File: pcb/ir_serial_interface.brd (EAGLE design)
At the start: 41.6 x 43.2 mm, 22 parts, among them IC1 PIC18F2550_28W, T1 SFH303

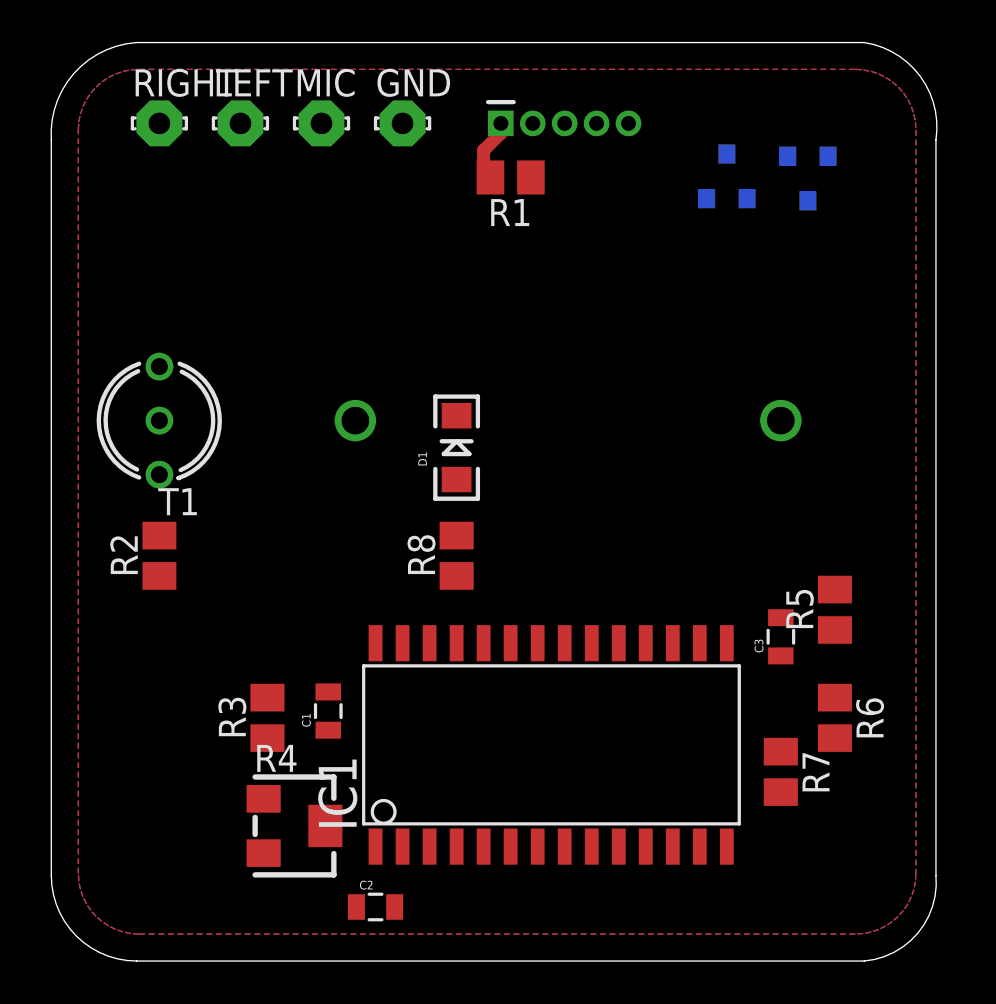
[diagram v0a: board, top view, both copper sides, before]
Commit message: RS232_TX working
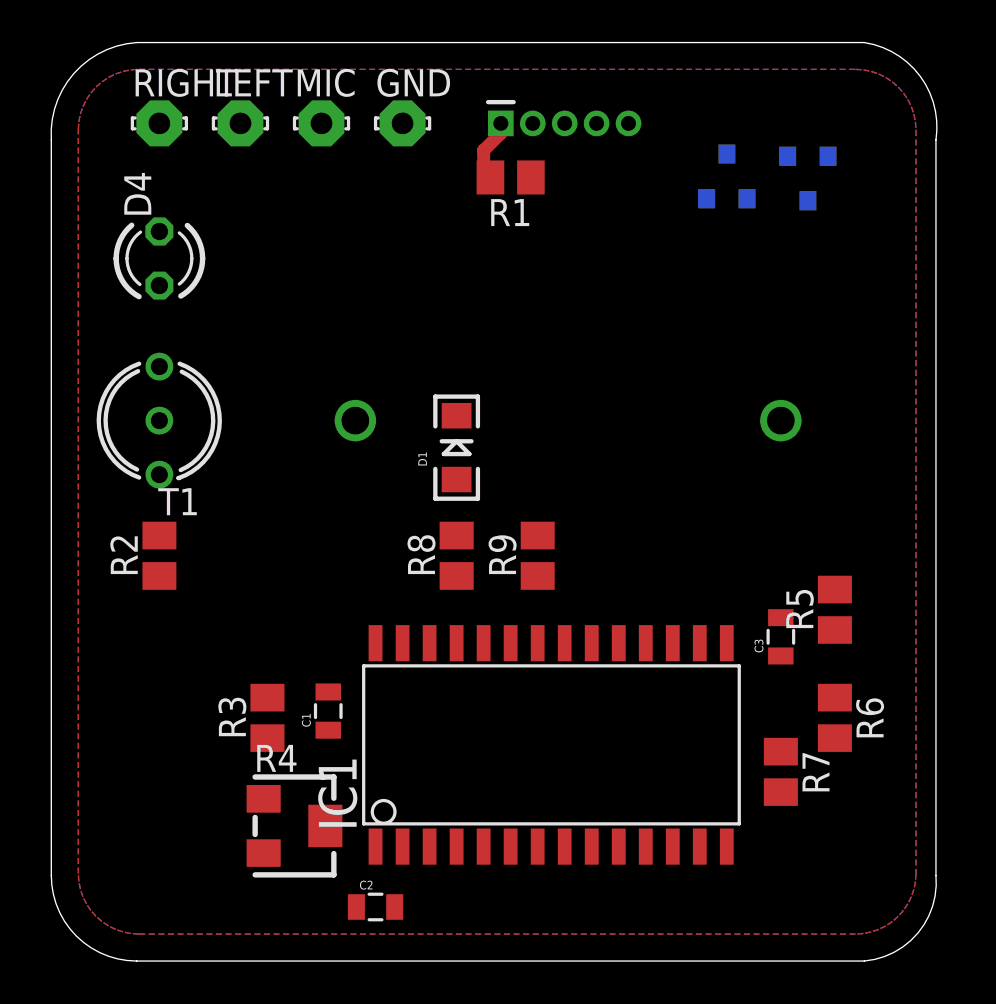
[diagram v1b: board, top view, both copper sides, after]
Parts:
- added D4: IR, led:LED3MM
- added R9: 190, resistor:M0805
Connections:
- new net N$14: D4.A, R9.2
- new net N$15: IC1.22, R9.1
- net GND: now also D4.K
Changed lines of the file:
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@@
 <?xml version="1.0" encoding="utf-8"?>
 <!DOCTYPE eagle SYSTEM "eagle.dtd">
-<eagle version="6.5.0">
+<eagle version="6.6.0">
 <drawing>
 <settings>
@@
 <element name="D3" library="SparkFun-DiscreteSemi" package="SOT23-3" value="" x="53.34" y="62.23" rot="MR0"/>
 <element name="R4" library="resistor" package="RTRIM3214W" value="200k" x="33.02" y="31.75" rot="R270"/>
+<element name="R9" library="resistor" package="M0805" value="190" x="44.45" y="44.45" rot="R90"/>
+<element name="D4" library="led" package="LED3MM" value="IR" x="26.67" y="58.42" rot="R90"/>
 </elements>
 <signals>
@@
 <contactref element="D3" pad="1"/>
 <contactref element="R4" pad="1"/>
+<contactref element="D4" pad="K"/>
+<wire x1="45.72" y1="64.77" x2="54.29" y2="61.23" width="0" layer="19" extent="16-16"/>
+<wire x1="38.1" y1="64.77" x2="45.72" y2="64.77" width="0" layer="19" extent="1-1"/>
+<wire x1="40.64" y1="51.03" x2="38.1" y2="64.77" width="0" layer="19" extent="1-1"/>
+<wire x1="48.26" y1="40.34" x2="40.64" y2="51.03" width="0" layer="19" extent="1-1"/>
+<wire x1="58.42" y1="40.96" x2="48.26" y2="40.34" width="0" layer="19" extent="1-1"/>
 <wire x1="58.42" y1="37.78" x2="58.42" y2="40.96" width="0" layer="19" extent="1-1"/>
-<wire x1="48.26" y1="40.34" x2="58.42" y2="40.96" width="0" layer="19" extent="1-1"/>
-<wire x1="40.64" y1="51.03" x2="48.26" y2="40.34" width="0" layer="19" extent="1-1"/>
-<wire x1="38.1" y1="64.77" x2="40.64" y2="51.03" width="0" layer="19" extent="1-1"/>
 <wire x1="26.67" y1="43.5" x2="40.64" y2="51.03" width="0" layer="19" extent="1-1"/>
 <wire x1="31.57" y1="33.025" x2="26.67" y2="43.5" width="0" layer="19" extent="1-1"/>
 <wire x1="35.93" y1="27.94" x2="31.57" y2="33.025" width="0" layer="19" extent="1-1"/>
+<wire x1="26.67" y1="59.69" x2="35.93" y2="27.94" width="0" layer="19" extent="1-1"/>
 </signal>
 <signal name="N$1">
@@
 <wire x1="53.34" y1="63.33" x2="56.2" y2="63.23" width="0" layer="19" extent="16-16"/>
 </signal>
+<signal name="N$14">
+<contactref element="D4" pad="A"/>
+<contactref element="R9" pad="2"/>
+<wire x1="26.67" y1="57.15" x2="44.45" y2="45.4" width="0" layer="19" extent="1-1"/>
+</signal>
+<signal name="N$15">
+<contactref element="R9" pad="1"/>
+<contactref element="IC1" pad="22"/>
+<wire x1="44.45" y1="43.5" x2="44.45" y2="40.34" width="0" layer="19" extent="1-1"/>
+</signal>
 </signals>

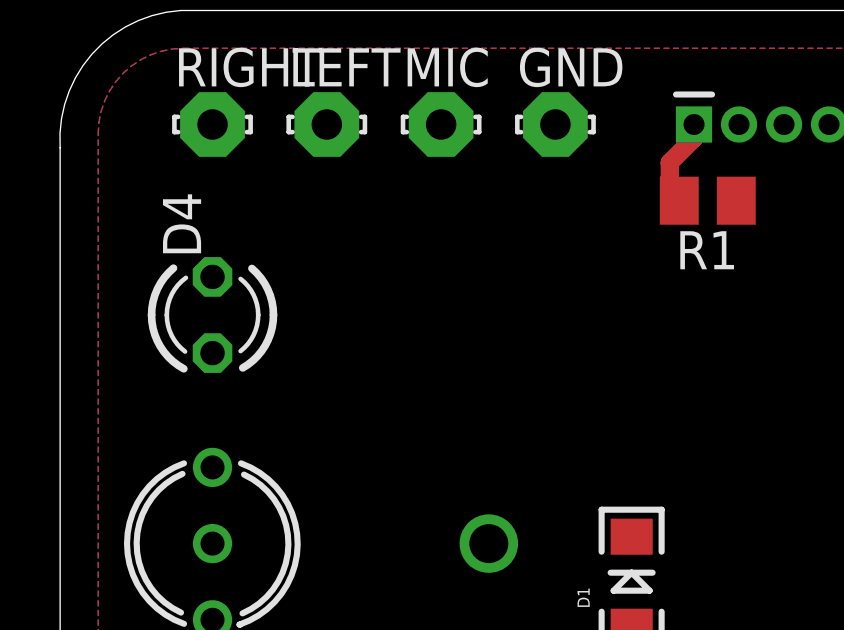
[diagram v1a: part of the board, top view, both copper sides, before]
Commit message: PCB: R channel enables MeterLogger
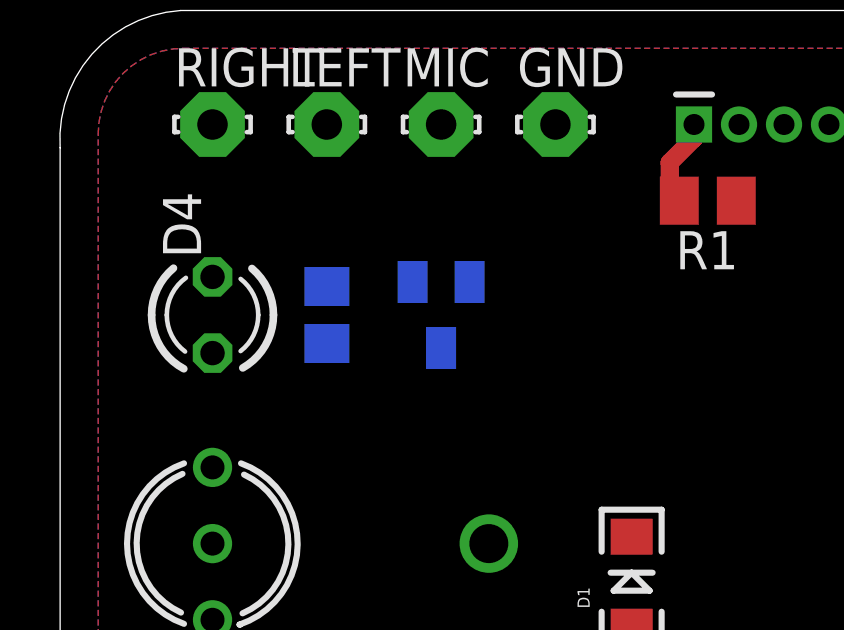
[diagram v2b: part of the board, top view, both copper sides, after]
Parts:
- added C4: (no value), rcl:C0805
- added Q1: BSS123, transistor-small-signal:SOT23
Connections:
- new net N$16: BAT1.1, Q1.3
- new net N$17: C4.1, Q1.1, RIGHT.MP
- net +5V: now also Q1.2; no longer BAT1.1
- net GND: now also C4.2
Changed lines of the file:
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@@
 <grid distance="0.05" unitdist="inch" unit="inch" style="dots" multiple="1" display="no" altdistance="0.025" altunitdist="inch" altunit="inch"/>
 <layers>
-<layer number="1" name="Top" color="4" fill="1" visible="yes" active="yes"/>
-<layer number="16" name="Bottom" color="1" fill="1" visible="no" active="yes"/>
+<layer number="1" name="Top" color="4" fill="1" visible="no" active="yes"/>
+<layer number="16" name="Bottom" color="1" fill="1" visible="yes" active="yes"/>
 <layer number="17" name="Pads" color="2" fill="1" visible="yes" active="yes"/>
 <layer number="18" name="Vias" color="2" fill="1" visible="yes" active="yes"/>
 <layer number="19" name="Unrouted" color="6" fill="1" visible="yes" active="yes"/>
 <layer number="20" name="Dimension" color="15" fill="1" visible="yes" active="yes"/>
-<layer number="21" name="tPlace" color="7" fill="1" visible="yes" active="yes"/>
-<layer number="22" name="bPlace" color="7" fill="1" visible="no" active="yes"/>
-<layer number="23" name="tOrigins" color="15" fill="1" visible="yes" active="yes"/>
-<layer number="24" name="bOrigins" color="15" fill="1" visible="no" active="yes"/>
-<layer number="25" name="tNames" color="7" fill="1" visible="yes" active="yes"/>
-<layer number="26" name="bNames" color="7" fill="1" visible="no" active="yes"/>
-<layer number="27" name="tValues" color="7" fill="1" visible="yes" active="yes"/>
-<layer number="28" name="bValues" color="7" fill="1" visible="no" active="yes"/>
-<layer number="29" name="tStop" color="7" fill="3" visible="yes" active="yes"/>
-<layer number="30" name="bStop" color="7" fill="6" visible="no" active="yes"/>
-<layer number="31" name="tCream" color="7" fill="4" visible="yes" active="yes"/>
-<layer number="32" name="bCream" color="7" fill="5" visible="no" active="yes"/>
-<layer number="33" name="tFinish" color="6" fill="3" visible="yes" active="yes"/>
-<layer number="34" name="bFinish" color="6" fill="6" visible="no" active="yes"/>
-<layer number="35" name="tGlue" color="7" fill="4" visible="yes" active="yes"/>
-<layer number="36" name="bGlue" color="7" fill="5" visible="no" active="yes"/>
-<layer number="37" name="tTest" color="7" fill="1" visible="yes" active="yes"/>
-<layer number="38" name="bTest" color="7" fill="1" visible="no" active="yes"/>
-<layer number="39" name="tKeepout" color="4" fill="11" visible="yes" active="yes"/>
-<layer number="40" name="bKeepout" color="1" fill="11" visible="no" active="yes"/>
-<layer number="41" name="tRestrict" color="4" fill="10" visible="yes" active="yes"/>
-<layer number="42" name="bRestrict" color="1" fill="10" visible="no" active="yes"/>
+<layer number="21" name="tPlace" color="7" fill="1" visible="no" active="yes"/>
+<layer number="22" name="bPlace" color="7" fill="1" visible="yes" active="yes"/>
+<layer number="23" name="tOrigins" color="15" fill="1" visible="no" active="yes"/>
+<layer number="24" name="bOrigins" color="15" fill="1" visible="yes" active="yes"/>
+<layer number="25" name="tNames" color="7" fill="1" visible="no" active="yes"/>
+<layer number="26" name="bNames" color="7" fill="1" visible="yes" active="yes"/>
+<layer number="27" name="tValues" color="7" fill="1" visible="no" active="yes"/>
+<layer number="28" name="bValues" color="7" fill="1" visible="yes" active="yes"/>
+<layer number="29" name="tStop" color="7" fill="3" visible="no" active="yes"/>
+<layer number="30" name="bStop" color="7" fill="6" visible="yes" active="yes"/>
+<layer number="31" name="tCream" color="7" fill="4" visible="no" active="yes"/>
+<layer number="32" name="bCream" color="7" fill="5" visible="yes" active="yes"/>
+<layer number="33" name="tFinish" color="6" fill="3" visible="no" active="yes"/>
+<layer number="34" name="bFinish" color="6" fill="6" visible="yes" active="yes"/>
+<layer number="35" name="tGlue" color="7" fill="4" visible="no" active="yes"/>
+<layer number="36" name="bGlue" color="7" fill="5" visible="yes" active="yes"/>
+<layer number="37" name="tTest" color="7" fill="1" visible="no" active="yes"/>
+<layer number="38" name="bTest" color="7" fill="1" visible="yes" active="yes"/>
+<layer number="39" name="tKeepout" color="4" fill="11" visible="no" active="yes"/>
+<layer number="40" name="bKeepout" color="1" fill="11" visible="yes" active="yes"/>
+<layer number="41" name="tRestrict" color="4" fill="10" visible="no" active="yes"/>
+<layer number="42" name="bRestrict" color="1" fill="10" visible="yes" active="yes"/>
 <layer number="43" name="vRestrict" color="2" fill="10" visible="yes" active="yes"/>
 <layer number="44" name="Drills" color="7" fill="1" visible="yes" active="yes"/>
@@
 <layer number="49" name="Reference" color="7" fill="1" visible="yes" active="yes"/>
 <layer number="50" name="dxf" color="7" fill="1" visible="no" active="no"/>
-<layer number="51" name="tDocu" color="7" fill="1" visible="yes" active="yes"/>
-<layer number="52" name="bDocu" color="7" fill="1" visible="no" active="yes"/>
+<layer number="51" name="tDocu" color="7" fill="1" visible="no" active="yes"/>
+<layer number="52" name="bDocu" color="7" fill="1" visible="yes" active="yes"/>
 <layer number="53" name="tGND_GNDA" color="7" fill="9" visible="no" active="no"/>
 <layer number="54" name="bGND_GNDA" color="1" fill="9" visible="no" active="no"/>
@@
 <layer number="103" name="tMap" color="7" fill="1" visible="yes" active="yes"/>
 <layer number="104" name="Name" color="16" fill="1" visible="yes" active="yes"/>
-<layer number="105" name="tPlate" color="7" fill="1" visible="yes" active="yes"/>
-<layer number="106" name="bPlate" color="7" fill="1" visible="no" active="yes"/>
+<layer number="105" name="tPlate" color="7" fill="1" visible="no" active="yes"/>
+<layer number="106" name="bPlate" color="7" fill="1" visible="yes" active="yes"/>
 <layer number="107" name="Crop" color="7" fill="1" visible="yes" active="yes"/>
 <layer number="108" name="tplace-old" color="10" fill="1" visible="no" active="yes"/>
 <layer number="109" name="ref-old" color="11" fill="1" visible="no" active="yes"/>
 <layer number="116" name="Patch_BOT" color="9" fill="4" visible="yes" active="yes"/>
-<layer number="121" name="_tsilk" color="7" fill="1" visible="yes" active="yes"/>
-<layer number="122" name="_bsilk" color="7" fill="1" visible="no" active="yes"/>
+<layer number="121" name="_tsilk" color="7" fill="1" visible="no" active="yes"/>
+<layer number="122" name="_bsilk" color="7" fill="1" visible="yes" active="yes"/>
 <layer number="125" name="_tNames" color="7" fill="1" visible="yes" active="yes"/>
 <layer number="144" name="Drill_legend" color="7" fill="1" visible="yes" active="yes"/>
@@
 <element name="R9" library="resistor" package="M0805" value="190" x="44.45" y="44.45" rot="R90"/>
 <element name="D4" library="led" package="LED3MM" value="IR" x="26.67" y="58.42" rot="R90"/>
+<element name="Q1" library="transistor-small-signal" package="SOT23" value="BSS123" x="34.29" y="58.42" rot="MR180"/>
+<element name="C4" library="rcl" package="C0805" value="" x="30.48" y="58.42" rot="MR270"/>
 </elements>
 <signals>
@@
 <contactref element="R3" pad="2"/>
 <contactref element="IC1" pad="20"/>
-<contactref element="BAT1" pad="1"/>
+<contactref element="Q1" pad="2"/>
+<wire x1="26.67" y1="50.8" x2="35.24" y2="59.52" width="0" layer="19" extent="16-16"/>
 </signal>
 <signal name="GND">
@@
 <contactref element="R4" pad="1"/>
 <contactref element="D4" pad="K"/>
+<contactref element="C4" pad="2"/>
 <wire x1="45.72" y1="64.77" x2="54.29" y2="61.23" width="0" layer="19" extent="16-16"/>
 <wire x1="38.1" y1="64.77" x2="45.72" y2="64.77" width="0" layer="19" extent="1-1"/>
-<wire x1="40.64" y1="51.03" x2="38.1" y2="64.77" width="0" layer="19" extent="1-1"/>
+<wire x1="30.48" y1="57.47" x2="38.1" y2="64.77" width="0" layer="19" extent="16-16"/>
+<wire x1="26.67" y1="59.69" x2="30.48" y2="57.47" width="0" layer="19" extent="16-16"/>
+<wire x1="40.64" y1="51.03" x2="30.48" y2="57.47" width="0" layer="19" extent="1-16"/>
 <wire x1="48.26" y1="40.34" x2="40.64" y2="51.03" width="0" layer="19" extent="1-1"/>
 <wire x1="58.42" y1="40.96" x2="48.26" y2="40.34" width="0" layer="19" extent="1-1"/>
 <wire x1="58.42" y1="37.78" x2="58.42" y2="40.96" width="0" layer="19" extent="1-1"/>
-<wire x1="26.67" y1="43.5" x2="40.64" y2="51.03" width="0" layer="19" extent="1-1"/>
+<wire x1="26.67" y1="43.5" x2="30.48" y2="57.47" width="0" layer="19" extent="1-16"/>
 <wire x1="31.57" y1="33.025" x2="26.67" y2="43.5" width="0" layer="19" extent="1-1"/>
 <wire x1="35.93" y1="27.94" x2="31.57" y2="33.025" width="0" layer="19" extent="1-1"/>
-<wire x1="26.67" y1="59.69" x2="35.93" y2="27.94" width="0" layer="19" extent="1-1"/>
 </signal>
 <signal name="N$1">
@@
 <contactref element="R9" pad="1"/>
 <contactref element="IC1" pad="22"/>
-<wire x1="44.45" y1="43.5" x2="44.45" y2="40.34" width="0" layer="19" extent="1-1"/>
+<wire x1="44.45" y1="40.34" x2="44.45" y2="43.5" width="0" layer="19" extent="1-1"/>
+</signal>
+<signal name="N$16">
+<contactref element="Q1" pad="3"/>
+<contactref element="BAT1" pad="1"/>
+<wire x1="35.88" y1="50.8" x2="34.29" y2="57.32" width="0" layer="19" extent="16-16"/>
+</signal>
+<signal name="N$17">
+<contactref element="RIGHT" pad="MP"/>
+<contactref element="Q1" pad="1"/>
+<contactref element="C4" pad="1"/>
+<wire x1="26.67" y1="64.77" x2="33.34" y2="59.52" width="0" layer="19" extent="16-16"/>
+<wire x1="30.48" y1="59.37" x2="33.34" y2="59.52" width="0" layer="19" extent="1-16"/>
 </signal>
 </signals>

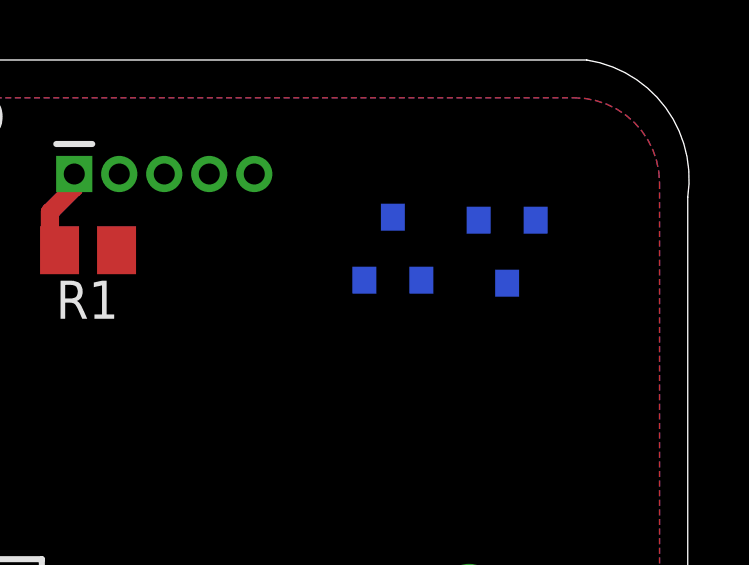
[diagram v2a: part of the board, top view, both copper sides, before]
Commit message: sleep longer after fsk tx
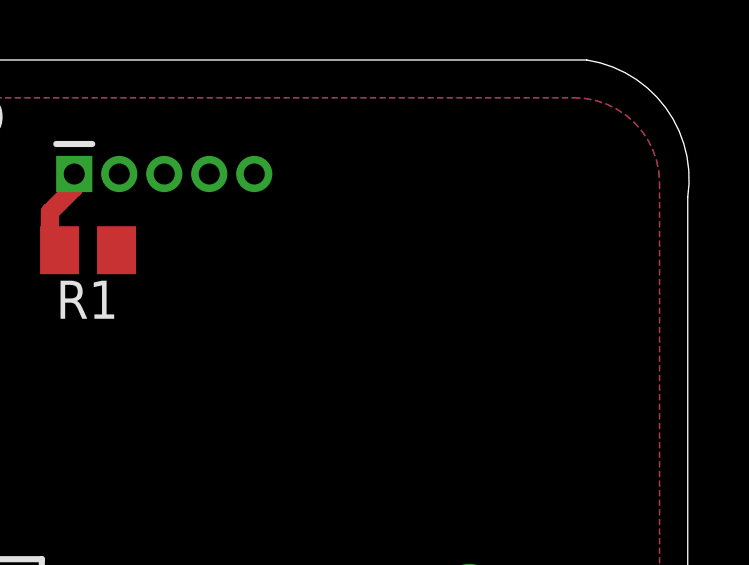
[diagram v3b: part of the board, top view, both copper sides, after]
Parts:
- removed D2, D3: (no value), SparkFun-DiscreteSemi:SOT23-3
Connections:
- removed net N$12: BAT1.2, D2.3
- removed net N$13: D2.1, D3.3
- new net -: BAT1.2
- net GND: no longer D3.1
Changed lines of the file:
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@@
 <element name="R8" library="resistor" package="M0805" value="190" x="40.64" y="44.45" rot="R90"/>
 <element name="BAT1" library="SparkFun-Electromechanical" package="BATTCOM_20MM_PTH" value="20mm coincell" x="55.88" y="50.8" rot="MR0"/>
-<element name="D2" library="SparkFun-DiscreteSemi" package="SOT23-3" value="" x="57.15" y="62.23" rot="MR180"/>
-<element name="D3" library="SparkFun-DiscreteSemi" package="SOT23-3" value="" x="53.34" y="62.23" rot="MR0"/>
 <element name="R4" library="resistor" package="RTRIM3214W" value="200k" x="33.02" y="31.75" rot="R270"/>
 <element name="R9" library="resistor" package="M0805" value="190" x="44.45" y="44.45" rot="R90"/>
@@
 <contactref element="R6" pad="1"/>
 <contactref element="D1" pad="C"/>
-<contactref element="D3" pad="1"/>
 <contactref element="R4" pad="1"/>
 <contactref element="D4" pad="K"/>
 <contactref element="C4" pad="2"/>
-<wire x1="45.72" y1="64.77" x2="54.29" y2="61.23" width="0" layer="19" extent="16-16"/>
 <wire x1="38.1" y1="64.77" x2="45.72" y2="64.77" width="0" layer="19" extent="1-1"/>
 <wire x1="30.48" y1="57.47" x2="38.1" y2="64.77" width="0" layer="19" extent="16-16"/>
@@
 <wire x1="40.64" y1="40.34" x2="40.64" y2="43.5" width="0" layer="19" extent="1-1"/>
 </signal>
-<signal name="N$12">
-<contactref element="BAT1" pad="2"/>
-<contactref element="D2" pad="3"/>
-<wire x1="55.88" y1="50.8" x2="57.15" y2="61.13" width="0" layer="19" extent="16-16"/>
-</signal>
-<signal name="N$13">
-<contactref element="D2" pad="1"/>
-<contactref element="D3" pad="3"/>
-<wire x1="53.34" y1="63.33" x2="56.2" y2="63.23" width="0" layer="19" extent="16-16"/>
-</signal>
 <signal name="N$14">
 <contactref element="D4" pad="A"/>
@@
 <wire x1="30.48" y1="59.37" x2="33.34" y2="59.52" width="0" layer="19" extent="1-16"/>
 </signal>
+<signal name="-">
+<contactref element="BAT1" pad="2"/>
+</signal>
 </signals>

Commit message: multical iii docs + pcb
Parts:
- R4: value 200k -> 100k; device resistor:RTRIM3214W -> resistor:M0805
- moved R4 1.27 mm to (31.8, 31.8), turned to 90 degrees
